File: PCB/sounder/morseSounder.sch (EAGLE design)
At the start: 84 parts, among them IC1 LM386M-1, IC5 LM321MF, J1 AVR_SPI_PRG_6PTH, J2 POWERPOLE_POWER25A_HORIZONTAL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, J3 POWER_JACKPTH, Q1 MMBT3904, Q2 MMBT3904, Q3 MMBT3904, Q4 2.5A/30V/105mΩ, Q5 MMBT3904, T1 MMBTA42, U1 ATMEGA328P_TQFP

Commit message: Rebuilt audio circuit to use a synthesised digital source rather than a tone generator.
Other improvements.

RGB power light/status indicator.
Better amplifier circuit.
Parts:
- removed C1, C3: 100u, SparkFun:CAP0805
- removed IC1: LM386M-1, linear:LM386M-1
- removed IC5: LM321MF, linear:LM321MF
- removed LED4: LED-902118128, morseSounder:LED-902118128
- removed Q1, Q2, Q3, Q5: MMBT3904, transistor:MMBT3904LT1-NPN-SOT23-BEC
- removed Q4: 2.5A/30V/105mΩ, SparkFun-DiscreteSemi:MOSFET_PCH-DMG2307L
- removed R12, R13, R14, R15, R30: 22K, SparkFun:RESISTOR0805-RES
- removed R17, R18: 10K, SparkFun:RESISTOR0805-RES
- removed R24: 4.7K, SparkFun:RESISTOR0805-RES
- removed R25, R26: 18K, SparkFun:RESISTOR0805-RES
- removed SJ1: SOLDERJUMPERNO, SparkFun:SOLDERJUMPERNO
- removed T1: MMBTA42, SparkFun:TRANSISTOR_NPNSOT23
- added C10, C11: 1n, SparkFun:CAP0805
- added C12: 1u, SparkFun:CAP0805
- added C21: 22p, SparkFun:CAP0805
- added D3: RGB, morseSounder:LED-RGB-CACREE
- added TP10, TP11, TP12, TP13, TP14, TP15: TEST-POINT3X5, SparkFun-Connectors:TEST-POINT3X5
- added U$10: MAX13331, morseSounder:MAX13331
- added U$8: SLP3SLP3, morseSounder:SLP3SLP3
- added U$9: DAC_MCP4725SOT, SparkFun:DAC_MCP4725SOT
- added Y1: (no value), SparkFun:CRYSTALHC49UV
- C13: value 0.018u -> 1u
- C14: value 0.018u -> 100n
- C15: value 0.047u -> 100n
- C16: value 0.047u -> 22p
- C2: value 200n -> 1u
- C4: value 100n -> 330n
- C5: value 10n -> 330n
- C6: value 100u -> 1n
- C7: value 100n -> 1u
- R1: value 1K -> 10K
- R10, R3, R9: value 10K -> 330
- R11: value 22K -> 10K
- R2: value 15K -> 10K
- R4, R5: value 10K -> 30K
- R6: value 10K -> 45K
- R7: value 330 -> 45K
- R8: value 330 -> 10K
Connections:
- removed net AUDIO_OUT: C1.1, C2.1, C3.1, IC1.OUT, TP4.1
- removed net AUDIO_PRE_AMP: C4.2, R3.1, TP5.1
- removed net AVR_KEY_OUT: R18.1, TP9.1, U1.PD3(INT1)
- removed net KEY_IN: Q4.D, R15.2, TP7.1
- removed net N$11: Q3.B, R7.2
- removed net N$12: C6.2, R10.1, R7.1, R8.2, R9.2
- removed net N$13: Q1.E, R11.2
- removed net N$14: SJ1.2, U$2.RING
- removed net N$24: C14.1, R26.1, T1.B
- removed net N$25: C15.1, C16.1, R25.1, R26.2
- removed net N$26: C13.1, C14.2, U$3G$1.A
- removed net N$36: LED4.A, R30.1
- removed net N$9: C7.2, Q1.B, R14.2, R15.1
- new net ADC_MAX13331_DIAG: C6.1, TP12.1, U$10.DIAG, U1.ADC6
- new net ADC_TONE: TP5.1, U$3G$1.S, U1.PC3(ADC3)
- new net ADC_VOLUME: TP4.1, U$3G$2.S, U1.PC2(ADC2)
- new net LED_FRONT_BLU: R9.1, TP14.1, U1.PD3(INT1)
- new net LED_FRONT_GRN: R10.1, TP15.1, U1.PD4(XCK/T0)
- new net LED_FRONT_RED: R3.1, TP13.1, U1.PD2(INT0)
- new net N$19: D3.RED, R3.2
- new net N$20: R8.1, TP11.1, U$10.SHDN
- new net OUT_L: C10.1, R7.1, U$10.OUTL, U$2.TIP
- new net OUT_R: C11.1, R6.1, U$10.OUTR, U$2.RING
- new net SCL: R1.1, TP6.1, U$9.SCL, U1.PC5(ADC5/SCL)
- new net SDA: R2.1, TP7.1, U$9.SDA, U1.PC4(ADC4/SDA)
- net +12V: no longer IC1.VS, IC5.V+, Q4.S, R12.1, R13.1, R17.2, R24.1, R5.1, R9.1
- net AVR_RESET: now also R11.2
- net AVR_VCC: now also C12.1, C14.1, C2.2, D3.A, R1.2, R11.1, R2.2, R8.2, TP10.1, U$10.CPVDD, U$10.VDD, U$3G$1.E, U$3G$2.E, U$9.VSS
- net GND: now also C10.2, C11.2, C12.2, C13.2, C14.2, C16.1, C2.1, C21.1, C6.2, U$10.PGND, U$10.PGND2, U$10.SGND, U$10.SGND2, U$3G$1.A, U$9.AO, U$9.VDD; no longer C2.2, C6.1, C7.1, IC1.-IN, IC1.GND, IC5.V-, LED4.C, Q5.E, R1.1, R10.2, R11.1, R14.1, R6.2, T1.E, U$3G$1.S
- net N$1: now also C21.2, U1.PB6(XTAL1/TOSC1), Y1.2; no longer C3.2, U$2.TIP
- net N$15: now also D3.BLU, R9.2; no longer R2.2, R3.2, TP8.1, U$3G$2.E, U$3G$2.S
- net N$16: now also C7.1, U$10.C1P; no longer Q5.B, R18.2
- net N$17: now also C7.2, U$10.C1N; no longer Q4.G, Q5.C, R17.1
- net N$2: now also C16.2, U1.PB7(XTAL2/TOSC2), Y1.1; no longer C1.2, SJ1.1
- net N$23: now also C13.1, C15.1, TP9.1, U$10.CPVSS, U$10.VSS; no longer C13.2, R24.2, R25.2, T1.C
- net N$3: now also D3.GRN, R10.2; no longer IC1.+IN, R1.2, R2.1
- net N$4: no longer R30.2
- net N$5: now also C4.2, R4.2; no longer C4.1, C5.2, IC5.OUT, R4.1
- net N$6: now also C5.2, R5.2; no longer C5.1, IC5.-IN, Q2.C, R12.2, R4.2
- net N$7: now also R4.1, R6.2, U$10.INR-; no longer IC5.+IN, Q3.C, R13.2, R5.2, R6.1
- net N$8: now also R5.1, R7.2, U$10.INL-; no longer Q1.C, Q2.E, Q3.E
- net TONE_OUT: now also C4.1, C5.1, TP8.1, U$9.VOUT; no longer C16.2, Q2.B, R8.1, TP6.1
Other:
- note added: "Amplifier"
- note added: "LEDs"
- note added: "Speaker and ouput connector"
- note added: "Tone"
- note added: "Tone generation DAC"
- note added: "Volume"
- note removed: "10K"
- note removed: "Audio amplifier"
- note removed: "High Side Driver for Level Shifting"
- note removed: "Level translator and key input select"
- note removed: "Short for stereo opperation"
- note removed: "Twin T oscilator"
- moved on the sheet: C13, C14, C15, C16, C2, C4, C5, C6, C7, C8, C9, J4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

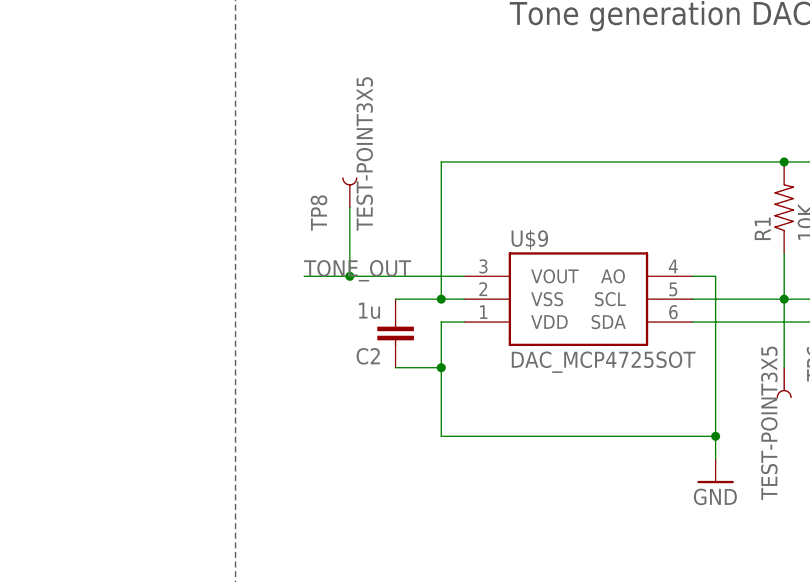
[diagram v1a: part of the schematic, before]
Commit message: Fixed Pinout of DAC chip
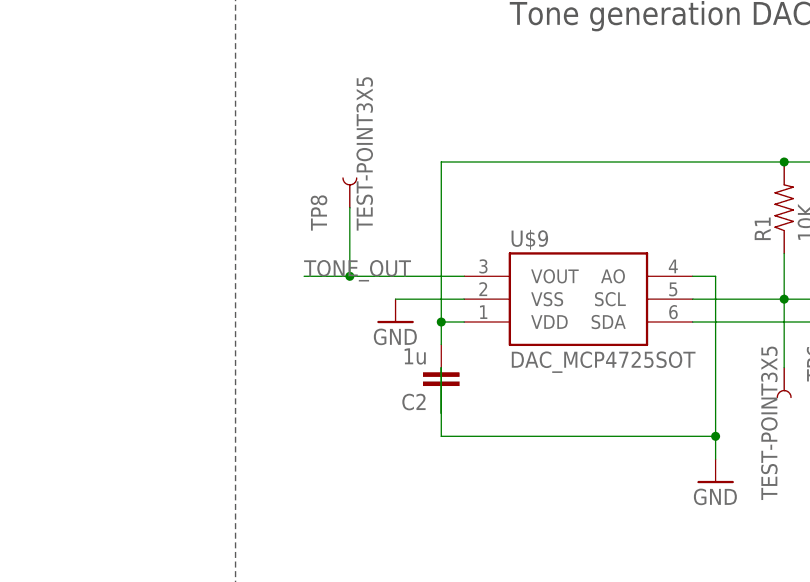
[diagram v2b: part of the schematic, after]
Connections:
- net AVR_VCC: now also U$9.VDD; no longer U$9.VSS
- net GND: now also U$9.VSS; no longer U$9.VDD
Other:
- moved on the sheet: C2
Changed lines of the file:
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@@
 <?xml version="1.0" encoding="utf-8"?>
 <!DOCTYPE eagle SYSTEM "eagle.dtd">
-<eagle version="6.5.0">
+<eagle version="9.1.3">
 <drawing>
 <settings>
 <setting alwaysvectorfont="no"/>
+<setting keepoldvectorfont="yes"/>
 <setting verticaltext="up"/>
 </settings>
@@
 <part name="R9" library="SparkFun" deviceset="RESISTOR" device="0805-RES" value="330"/>
 <part name="R10" library="SparkFun" deviceset="RESISTOR" device="0805-RES" value="330"/>
+<part name="GND13" library="supply1" deviceset="GND" device=""/>
 </parts>
 <sheets>
@@
 <instance part="R2" gate="G$1" x="243.84" y="175.26" rot="R90"/>
 <instance part="GND5" gate="1" x="226.06" y="144.78"/>
-<instance part="C2" gate="G$1" x="190.5" y="162.56" rot="R180"/>
+<instance part="C2" gate="G$1" x="195.58" y="157.48" rot="R180"/>
 <instance part="TP6" gate="G$1" x="233.68" y="157.48" rot="R270"/>
 <instance part="TP7" gate="G$1" x="243.84" y="157.48" rot="R270"/>
@@
 <instance part="R9" gate="G$1" x="208.28" y="241.3"/>
 <instance part="R10" gate="G$1" x="208.28" y="238.76"/>
+<instance part="GND13" gate="1" x="190.5" y="162.56"/>
 </instances>
 <busses>
@@
 <pinref part="GND5" gate="1" pin="GND"/>
 <wire x1="226.06" y1="147.32" x2="226.06" y2="149.86" width="0.1524" layer="91"/>
-<pinref part="U$9" gate="G$1" pin="VDD"/>
-<wire x1="198.12" y1="162.56" x2="195.58" y2="162.56" width="0.1524" layer="91"/>
-<wire x1="195.58" y1="162.56" x2="195.58" y2="157.48" width="0.1524" layer="91"/>
 <wire x1="195.58" y1="157.48" x2="195.58" y2="149.86" width="0.1524" layer="91"/>
 <wire x1="195.58" y1="149.86" x2="226.06" y2="149.86" width="0.1524" layer="91"/>
 <pinref part="C2" gate="G$1" pin="1"/>
-<wire x1="190.5" y1="157.48" x2="195.58" y2="157.48" width="0.1524" layer="91"/>
-<junction x="195.58" y="157.48"/>
+<wire x1="195.58" y1="152.4" x2="195.58" y2="157.48" width="0.1524" layer="91"/>
 <pinref part="U$9" gate="G$1" pin="AO"/>
 <wire x1="223.52" y1="167.64" x2="226.06" y2="167.64" width="0.1524" layer="91"/>
@@
 <wire x1="195.58" y1="66.04" x2="203.2" y2="66.04" width="0.1524" layer="91"/>
 <junction x="195.58" y="66.04"/>
+</segment>
+<segment>
+<pinref part="U$9" gate="G$1" pin="VSS"/>
+<pinref part="GND13" gate="1" pin="GND"/>
+<wire x1="198.12" y1="165.1" x2="190.5" y2="165.1" width="0.1524" layer="91"/>
 </segment>
 </net>
@@
 <pinref part="R2" gate="G$1" pin="2"/>
 <wire x1="238.76" y1="180.34" x2="243.84" y2="180.34" width="0.1524" layer="91"/>
-<pinref part="U$9" gate="G$1" pin="VSS"/>
-<wire x1="198.12" y1="165.1" x2="195.58" y2="165.1" width="0.1524" layer="91"/>
-<wire x1="195.58" y1="165.1" x2="195.58" y2="180.34" width="0.1524" layer="91"/>
+<wire x1="195.58" y1="162.56" x2="195.58" y2="180.34" width="0.1524" layer="91"/>
 <wire x1="195.58" y1="180.34" x2="233.68" y2="180.34" width="0.1524" layer="91"/>
 <pinref part="C2" gate="G$1" pin="2"/>
-<wire x1="190.5" y1="165.1" x2="195.58" y2="165.1" width="0.1524" layer="91"/>
-<junction x="195.58" y="165.1"/>
+<wire x1="195.58" y1="160.02" x2="195.58" y2="162.56" width="0.1524" layer="91"/>
 <junction x="233.68" y="180.34"/>
 <junction x="238.76" y="180.34"/>
-</segment>
-<segment>
+<pinref part="U$9" gate="G$1" pin="VDD"/>
+<wire x1="198.12" y1="162.56" x2="195.58" y2="162.56" width="0.1524" layer="91"/>
+<junction x="195.58" y="162.56"/>
+</segment>
+<segment>

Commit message: Added document frame to the Sounder Schematic
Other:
- note added: "Morse Sounder"
- note added: "Revision: R2.1"
- moved on the sheet: C10, C11, C12, C13, C14, C15, C16, C17, C18, C19, C2, C20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

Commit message: Flip weight and rate controls to match front pannel
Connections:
- net ADC_RATE: now also TP2.1, U$6G$2.S, U1.PC0(ADC0); no longer TP1.1, U$6G$1.S, U1.PC1(ADC1)
- net ADC_WEIGHT: now also TP1.1, U$6G$1.S, U1.PC1(ADC1); no longer TP2.1, U$6G$2.S, U1.PC0(ADC0)
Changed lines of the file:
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@@
 </segment>
 </net>
-<net name="ADC_RATE" class="0">
+<net name="ADC_WEIGHT" class="0">
 <segment>
 <pinref part="U$6" gate="G$1" pin="S"/>
@@
 </segment>
 </net>
-<net name="ADC_WEIGHT" class="0">
+<net name="ADC_RATE" class="0">
 <segment>
 <pinref part="U$6" gate="G$2" pin="S"/>

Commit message: Update component values to reduce volume and remove output distortion
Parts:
- C13, C7: value 1u -> 10u
- C14: value 100n -> 10u
- R4, R5: value 30K -> 62K
- R6, R7: value 45K -> 24K
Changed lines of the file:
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@@
 <part name="C4" library="SparkFun" deviceset="CAP" device="0805" value="330n"/>
 <part name="C5" library="SparkFun" deviceset="CAP" device="0805" value="330n"/>
-<part name="R4" library="SparkFun" deviceset="RESISTOR" device="0805-RES" value="30K"/>
-<part name="R5" library="SparkFun" deviceset="RESISTOR" device="0805-RES" value="30K"/>
-<part name="R6" library="SparkFun" deviceset="RESISTOR" device="0805-RES" value="45K"/>
-<part name="R7" library="SparkFun" deviceset="RESISTOR" device="0805-RES" value="45K"/>
+<part name="R4" library="SparkFun" deviceset="RESISTOR" device="0805-RES" value="62K"/>
+<part name="R5" library="SparkFun" deviceset="RESISTOR" device="0805-RES" value="62K"/>
+<part name="R6" library="SparkFun" deviceset="RESISTOR" device="0805-RES" value="24K"/>
+<part name="R7" library="SparkFun" deviceset="RESISTOR" device="0805-RES" value="24K"/>
 <part name="C6" library="SparkFun" deviceset="CAP" device="0805" value="1n"/>
-<part name="C7" library="SparkFun" deviceset="CAP" device="0805" value="1u"/>
+<part name="C7" library="SparkFun" deviceset="CAP" device="0805" value="10u"/>
 <part name="GND6" library="supply1" library_urn="urn:adsk.eagle:library:371" deviceset="GND" device=""/>
 <part name="GND7" library="supply1" library_urn="urn:adsk.eagle:library:371" deviceset="GND" device=""/>
@@
 <part name="R8" library="SparkFun" deviceset="RESISTOR" device="0805-RES" value="10K"/>
 <part name="C12" library="SparkFun" deviceset="CAP" device="0805" value="1u"/>
-<part name="C13" library="SparkFun" deviceset="CAP" device="0805" value="1u"/>
-<part name="C14" library="SparkFun" deviceset="CAP" device="0805" value="100n"/>
+<part name="C13" library="SparkFun" deviceset="CAP" device="0805" value="10u"/>
+<part name="C14" library="SparkFun" deviceset="CAP" device="0805" value="10u"/>
 <part name="C15" library="SparkFun" deviceset="CAP" device="0805" value="100n"/>
 <part name="GND14" library="supply1" library_urn="urn:adsk.eagle:library:371" deviceset="GND" device=""/>
